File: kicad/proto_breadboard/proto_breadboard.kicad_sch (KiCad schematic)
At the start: 22 parts, among them J1 ISP header, Q1 2N7000, SW1 SW_DPDT_x2, SW2 SW_MEC_5G, SW3 SW_MEC_5G, SW4 SW_MEC_5G, SW5 SW_MEC_5G, U1 GPD340, U2 ATtiny10, U3 12V boost converter

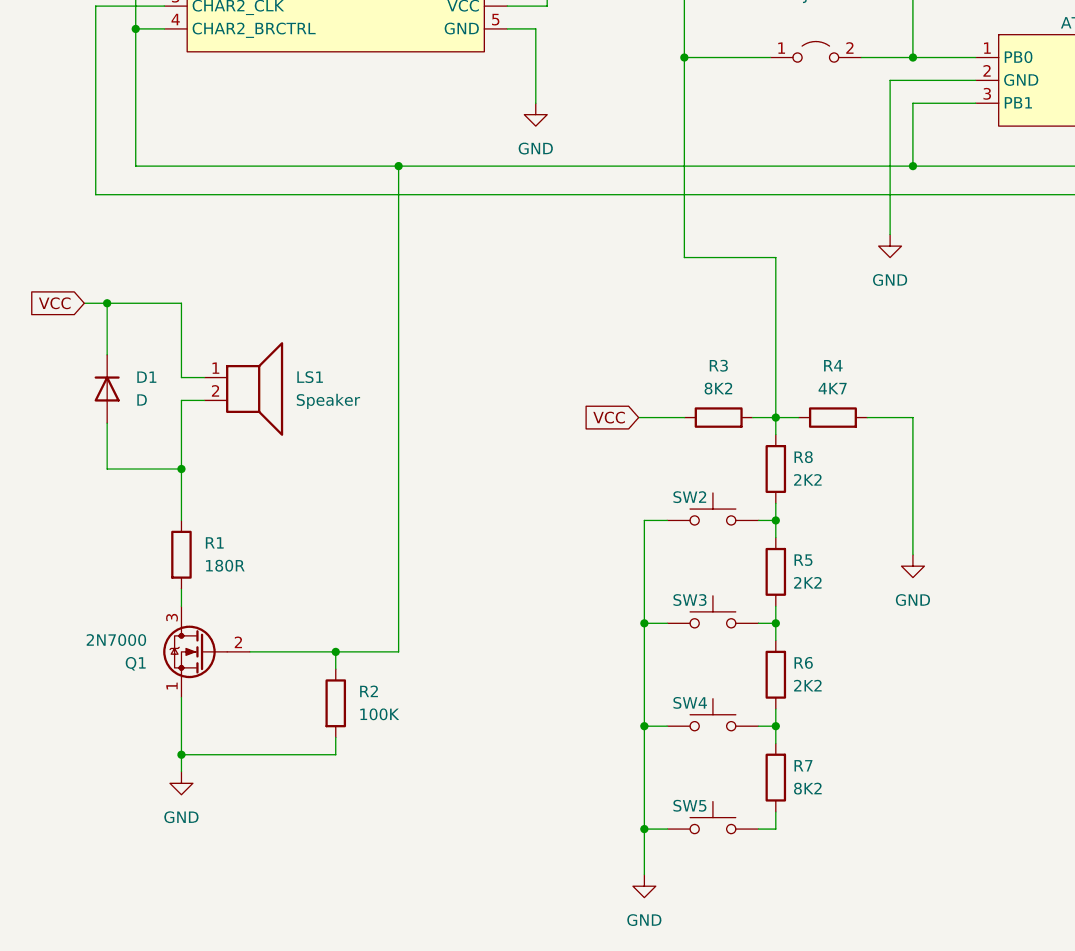
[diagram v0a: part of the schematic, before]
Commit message: drive speaker directly
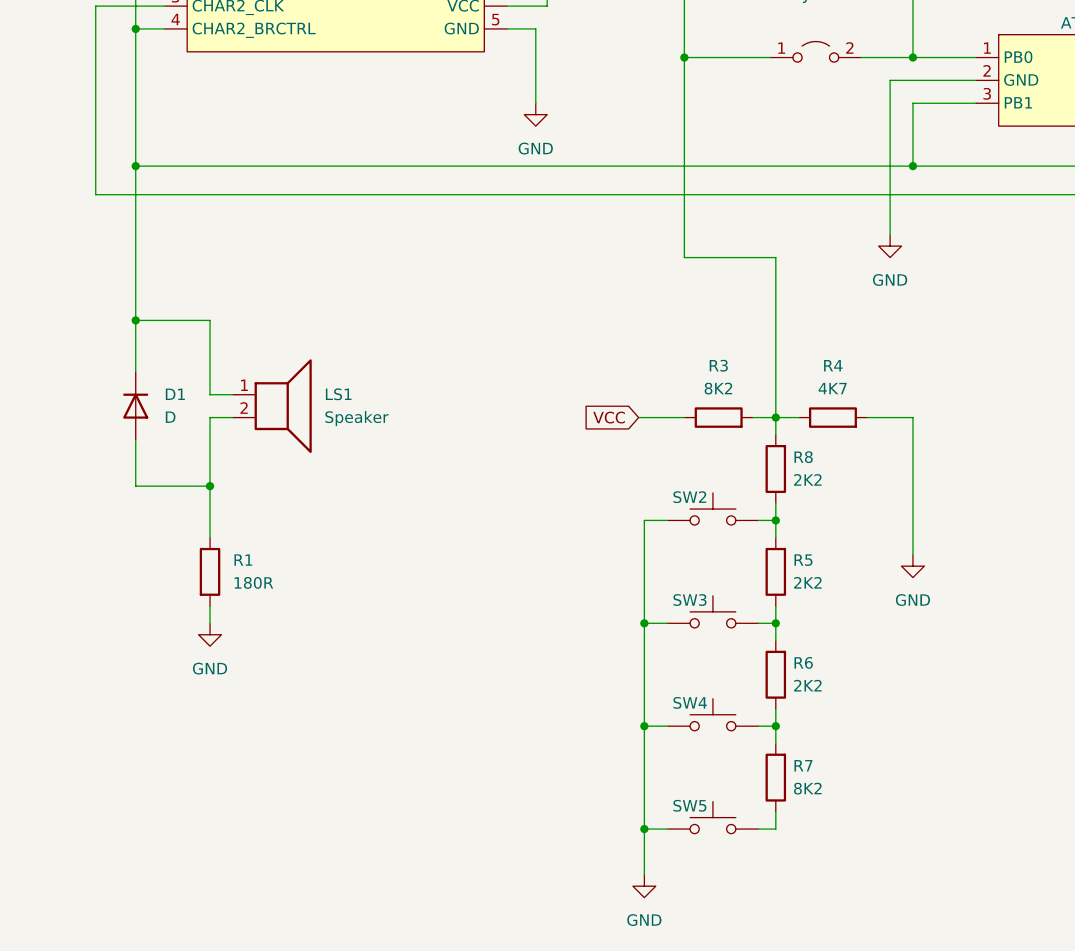
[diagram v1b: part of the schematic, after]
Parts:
- removed Q1: 2N7000, Package_TO_SOT_THT:TO-92_Inline, symbol Transistor_FET:2N7000
- removed R2: 100K, symbol Device:R
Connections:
- net CLK: now also D1.1 (K), LS1.1
- net GND: now also R1.2
- net VCC: no longer D1.1 (K), LS1.1
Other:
- moved on the sheet: D1, LS1, R1
